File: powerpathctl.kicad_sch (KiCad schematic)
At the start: 10 parts, among them J4 Conn_01x03_Male_BAT_PWR, J5 Conn_01x06_Male, J6 Conn_01x03_Male_BAT_PWR_IN_NU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, J7 Conn_01x06_Male_BAT_data, Q1 SI7149ADP-T1-GE3, U9 LTC4412ES6

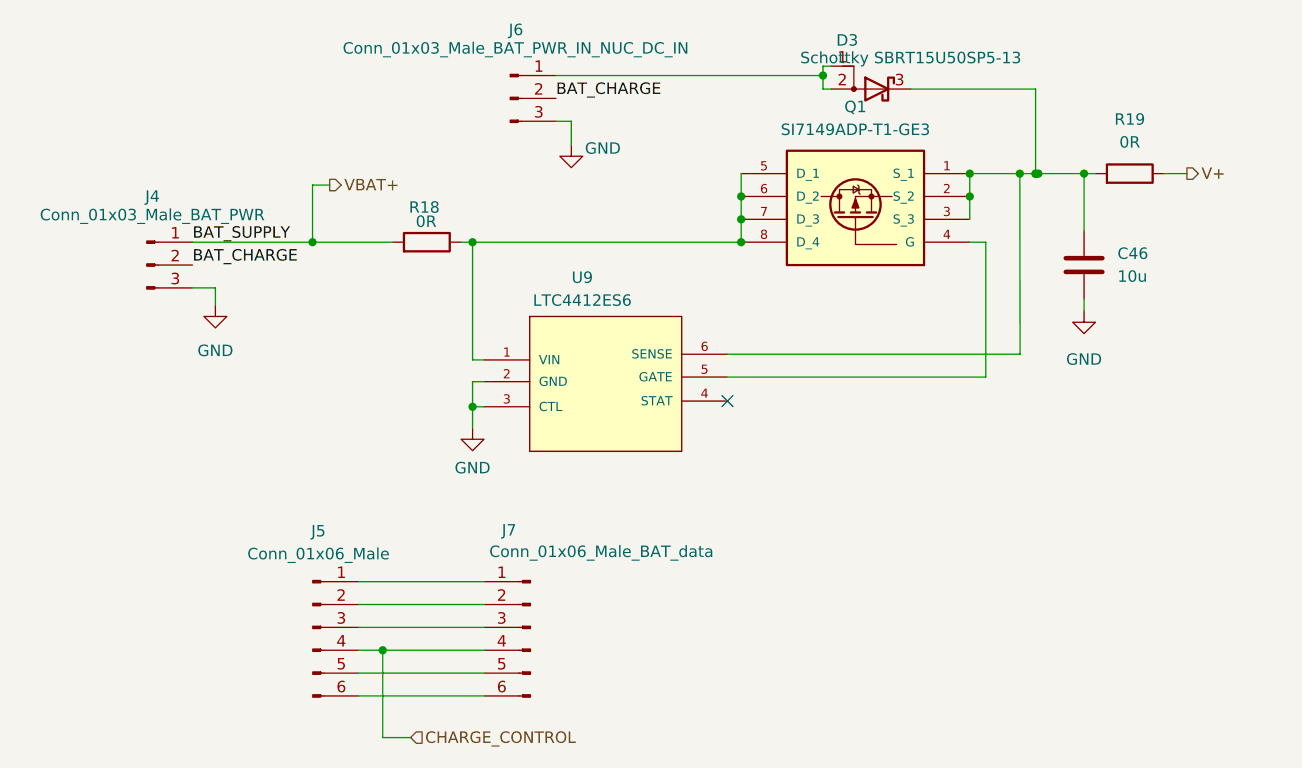
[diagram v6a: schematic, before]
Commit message: replaced main MCU, reannotated
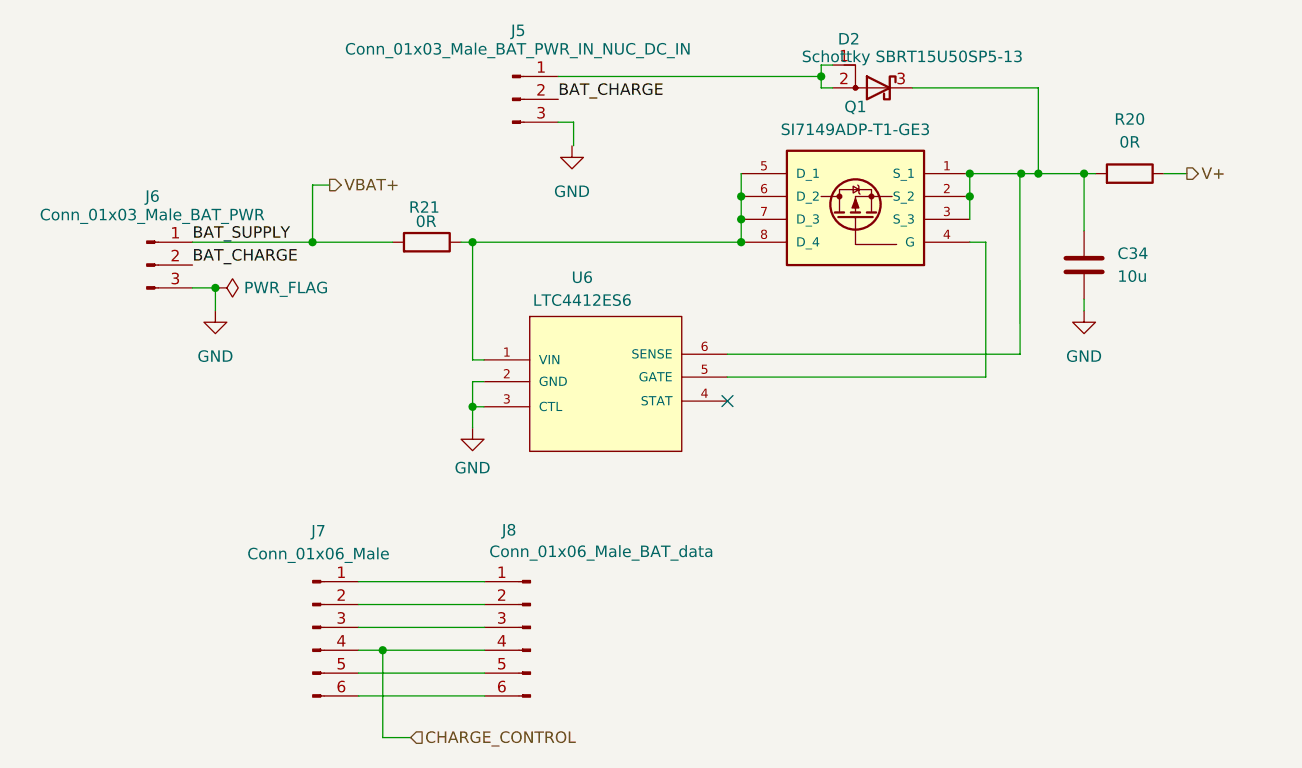
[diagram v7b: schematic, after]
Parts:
- renumbered C46 to C34, D3 to D2, J6 to J5, J4 to J6, J5 to J7, J7 to J8, R19 to R20, R18 to R21, U9 to U6
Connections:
- net GND: no longer J5.3 (Pin_3)
- net at Q1.1 (S_1), Q1.2 (S_2), Q1.3 (S_3)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: no longer C34.1, D2.3 (K), R20.2
- new net: C34.1, D2.3 (K), R20.2

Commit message: resolved all erc errors
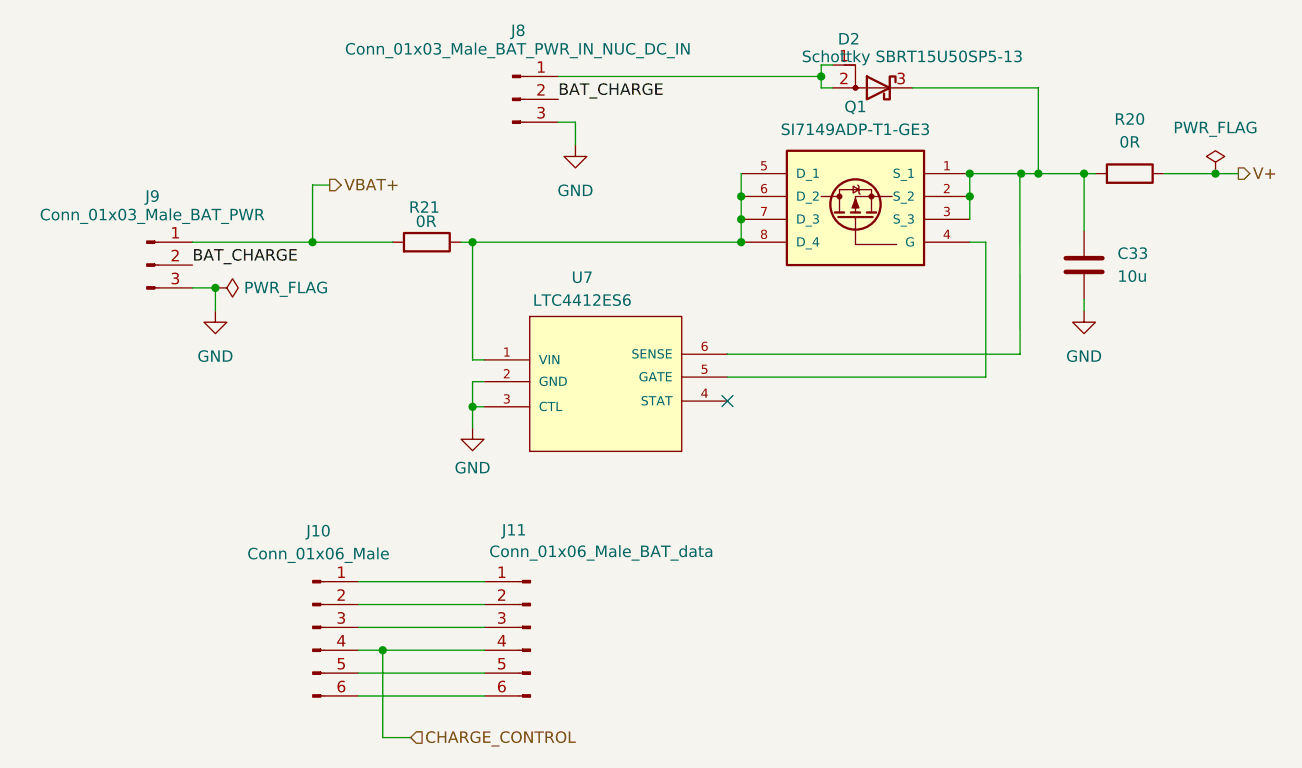
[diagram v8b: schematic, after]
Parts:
- renumbered C34 to C33, J7 to J10, J8 to J11, J5 to J8, J6 to J9, U6 to U7
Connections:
- net GND: now also J8.3 (Pin_3)
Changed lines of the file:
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@@
   (junction (at 176.53 69.85) (diameter 0) (color 0 0 0 0)
   )
+  (junction (at 203.835 67.31) (diameter 0) (color 0 0 0 0)
+  )
   (junction (at 121.285 74.93) (diameter 0) (color 0 0 0 0)
   )
@@
   (junction (at 103.505 74.93) (diameter 0) (color 0 0 0 0)
   )
+  (junction (at 92.71 80.01) (diameter 0) (color 0 0 0 0)
+  )
   (junction (at 182.245 67.31) (diameter 0) (color 0 0 0 0)
   )
   (junction (at 151.13 72.39) (diameter 0) (color 0 0 0 0)
   )
-  (junction (at 92.71 80.01) (diameter 0) (color 0 0 0 0)
-  )
   (no_connect (at 149.606 92.583))
+  (wire (pts (xy 132.715 61.595) (xy 132.715 64.135))
+    (stroke (width 0) (type default) (color 0 0 0 0))
+  )
   (wire (pts (xy 108.6104 117.729) (xy 122.6312 117.729))
     (stroke (width 0) (type default) (color 0 0 0 0))
@@
     (stroke (width 0) (type default) (color 0 0 0 0))
   )
-  (wire (pts (xy 130.81 61.595) (xy 132.5118 61.595))
-    (stroke (width 0) (type default) (color 0 0 0 0))
-  )
   (wire (pts (xy 121.285 90.424) (xy 121.285 93.218))
     (stroke (width 0) (type default) (color 0 0 0 0))
@@
     (stroke (width 0) (type default) (color 0 0 0 0))
   )
-  (wire (pts (xy 132.5118 61.595) (xy 132.5118 64.2112))
-    (stroke (width 0) (type default) (color 0 0 0 0))
-  )
   (wire (pts (xy 121.285 93.218) (xy 122.555 93.218))
     (stroke (width 0) (type default) (color 0 0 0 0))
@@
     (stroke (width 0) (type default) (color 0 0 0 0))
   )
-  (wire (pts (xy 198.12 67.31) (xy 200.66 67.31))
-    (stroke (width 0) (type default) (color 0 0 0 0))
-  )
   (wire (pts (xy 151.13 69.85) (xy 151.13 72.39))
     (stroke (width 0) (type default) (color 0 0 0 0))
@@
     (stroke (width 0) (type default) (color 0 0 0 0))
   )
+  (wire (pts (xy 198.12 67.31) (xy 203.835 67.31))
+    (stroke (width 0) (type default) (color 0 0 0 0))
+  )
   (wire (pts (xy 105.41 68.58) (xy 103.505 68.58))
     (stroke (width 0) (type default) (color 0 0 0 0))
@@
     (stroke (width 0) (type default) (color 0 0 0 0))
   )
+  (wire (pts (xy 203.835 67.31) (xy 206.375 67.31))
+    (stroke (width 0) (type default) (color 0 0 0 0))
+  )
   (wire (pts (xy 108.6104 112.649) (xy 122.6312 112.649))
+    (stroke (width 0) (type default) (color 0 0 0 0))
+  )
+  (wire (pts (xy 130.81 61.595) (xy 132.715 61.595))
     (stroke (width 0) (type default) (color 0 0 0 0))
   )
@@
     (effects (font (size 1.27 1.27)) (justify left bottom))
   )
-  (label "BAT_SUPPLY" (at 90.17 74.93 0)
-    (effects (font (size 1.27 1.27)) (justify left bottom))
-  )
   (hierarchical_label "CHARGE_CONTROL" (shape input) (at 114.4016 129.9718 0)
     (effects (font (size 1.27 1.27)) (justify left))
   )
-  (hierarchical_label "V+" (shape output) (at 200.66 67.31 0)
+  (hierarchical_label "V+" (shape output) (at 206.375 67.31 0)
     (effects (font (size 1.27 1.27)) (justify left))
   )
@@
   (symbol (lib_id "Connector:Conn_01x03_Male") (at 85.09 77.47 0) (unit 1)
     (in_bom yes) (on_board yes)
-    (property "Reference" "J6" (id 0) (at 85.725 69.85 0))
+    (property "Reference" "J9" (id 0) (at 85.725 69.85 0))
     (property "Value" "Conn_01x03_Male_BAT_PWR" (id 1) (at 85.6996 71.9074 0))
     (property "Footprint" "Connector_AMASS:AMASS_MR30PW-M_1x03_P3.50mm_Horizontal" (id 2) (at 85.09 77.47 0)
@@
   (symbol (lib_id "power:GND") (at 92.71 82.55 0) (unit 1)
     (in_bom yes) (on_board yes) (fields_autoplaced)
-    (property "Reference" "#PWR053" (id 0) (at 92.71 88.9 0)
+    (property "Reference" "#PWR049" (id 0) (at 92.71 88.9 0)
       (effects (font (size 1.27 1.27)) hide)
     )
@@
     (pin "2")
   )
-  (symbol (lib_id "power:PWR_FLAG") (at 92.71 80.01 270) (unit 1)
-    (in_bom yes) (on_board yes) (fields_autoplaced)
-    (property "Reference" "#FLG0101" (id 0) (at 94.615 80.01 0)
-      (effects (font (size 1.27 1.27)) hide)
-    )
-    (property "Value" "PWR_FLAG" (id 1) (at 95.885 80.0099 90)
-      (effects (font (size 1.27 1.27)) (justify left))
-    )
-    (property "Footprint" "" (id 2) (at 92.71 80.01 0)
-      (effects (font (size 1.27 1.27)) hide)
-    )
-    (property "Datasheet" "~" (id 3) (at 92.71 80.01 0)
-      (effects (font (size 1.27 1.27)) hide)
-    )
-    (pin "1")
-  )
   (symbol (lib_id "LTC4412ES6:LTC4412ES6") (at 127.635 83.185 0) (unit 1)
     (in_bom yes) (on_board yes)
-    (property "Reference" "U6" (id 0) (at 133.477 78.867 0))
+    (property "Reference" "U7" (id 0) (at 133.477 78.867 0))
     (property "Value" "LTC4412ES6" (id 1) (at 133.477 81.407 0))
     (property "Footprint" "Robotont:TSOT-23_S6" (id 2) (at 120.015 88.011 0)
@@
   (symbol (lib_id "Device:C") (at 189.23 77.47 0) (unit 1)
     (in_bom yes) (on_board yes) (fields_autoplaced)
-    (property "Reference" "C34" (id 0) (at 192.9384 76.1999 0)
+    (property "Reference" "C33" (id 0) (at 192.9384 76.1999 0)
       (effects (font (size 1.27 1.27)) (justify left))
     )
@@
     (pin "2")
   )
-  (symbol (lib_id "power:GND") (at 132.334 64.2366 0) (unit 1)
-    (in_bom yes) (on_board yes) (fields_autoplaced)
-    (property "Reference" "#PWR052" (id 0) (at 132.334 70.5866 0)
-      (effects (font (size 1.27 1.27)) hide)
-    )
-    (property "Value" "GND" (id 1) (at 132.334 69.3166 0))
-    (property "Footprint" "" (id 2) (at 132.334 64.2366 0)
-      (effects (font (size 1.27 1.27)) hide)
-    )
-    (property "Datasheet" "" (id 3) (at 132.334 64.2366 0)
+  (symbol (lib_id "power:GND") (at 132.715 64.135 0) (unit 1)
+    (in_bom yes) (on_board yes) (fields_autoplaced)
+    (property "Reference" "#PWR048" (id 0) (at 132.715 70.485 0)
+      (effects (font (size 1.27 1.27)) hide)
+    )
+    (property "Value" "GND" (id 1) (at 132.715 69.215 0))
+    (property "Footprint" "" (id 2) (at 132.715 64.135 0)
+      (effects (font (size 1.27 1.27)) hide)
+    )
+    (property "Datasheet" "" (id 3) (at 132.715 64.135 0)
       (effects (font (size 1.27 1.27)) hide)
     )
@@
   (symbol (lib_id "Connector:Conn_01x03_Male") (at 125.73 59.055 0) (unit 1)
     (in_bom yes) (on_board yes)
-    (property "Reference" "J5" (id 0) (at 126.365 51.435 0))
+    (property "Reference" "J8" (id 0) (at 126.365 51.435 0))
     (property "Value" "Conn_01x03_Male_BAT_PWR_IN_NUC_DC_IN" (id 1) (at 126.3396 53.4924 0))
     (property "Footprint" "Connector_AMASS:AMASS_MR30PW-M_1x03_P3.50mm_Horizontal" (id 2) (at 125.73 59.055 0)
@@
     (pin "3")
   )
+  (symbol (lib_id "power:PWR_FLAG") (at 203.835 67.31 0) (unit 1)
+    (in_bom yes) (on_board yes) (fields_autoplaced)
+    (property "Reference" "#FLG05" (id 0) (at 203.835 65.405 0)
+      (effects (font (size 1.27 1.27)) hide)
+    )
+    (property "Value" "PWR_FLAG" (id 1) (at 203.835 62.23 0))
+    (property "Footprint" "" (id 2) (at 203.835 67.31 0)
+      (effects (font (size 1.27 1.27)) hide)
+    )
+    (property "Datasheet" "~" (id 3) (at 203.835 67.31 0)
+      (effects (font (size 1.27 1.27)) hide)
+    )
+    (pin "1")
+  )
   (symbol (lib_id "Connector:Conn_01x06_Male") (at 127.7112 117.729 0) (mirror y) (unit 1)
     (in_bom yes) (on_board yes)
-    (property "Reference" "J8" (id 0) (at 124.5362 106.934 0)
+    (property "Reference" "J11" (id 0) (at 124.5362 106.934 0)
       (effects (font (size 1.27 1.27)) (justify right))
     )
@@
   (symbol (lib_id "power:GND") (at 189.23 82.55 0) (unit 1)
     (in_bom yes) (on_board yes) (fields_autoplaced)
-    (property "Reference" "#PWR054" (id 0) (at 189.23 88.9 0)
+    (property "Reference" "#PWR050" (id 0) (at 189.23 88.9 0)
       (effects (font (size 1.27 1.27)) hide)
     )
@@
     (pin "1")
   )
-  (symbol (lib_name "Conn_01x06_Male_1") (lib_id "Connector:Conn_01x06_Male") (at 103.5304 117.729 0) (unit 1)
-    (in_bom yes) (on_board yes) (fields_autoplaced)
-    (property "Reference" "J7" (id 0) (at 104.1654 107.0356 0))
+  (symbol (lib_id "Connector:Conn_01x06_Male") (at 103.5304 117.729 0) (unit 1)
+    (in_bom yes) (on_board yes) (fields_autoplaced)
+    (property "Reference" "J10" (id 0) (at 104.1654 107.0356 0))
     (property "Value" "Conn_01x06_Male " (id 1) (at 104.1654 109.5756 0))
     (property "Footprint" "Connector_JST:JST_PH_S6B-PH-K_1x06_P2.00mm_Horizontal" (id 2) (at 103.5304 117.729 0)
       (effects (font (size 1.27 1.27)) hide)
     )
-    (property "Datasheet" "" (id 3) (at 104.4448 118.6942 0)
+    (property "Datasheet" "~" (id 3) (at 104.4448 118.6942 0)
       (effects (font (size 1.27 1.27)) hide)
     )
@@
   (symbol (lib_id "power:GND") (at 121.285 95.5548 0) (unit 1)
     (in_bom yes) (on_board yes) (fields_autoplaced)
-    (property "Reference" "#PWR055" (id 0) (at 121.285 101.9048 0)
+    (property "Reference" "#PWR051" (id 0) (at 121.285 101.9048 0)
       (effects (font (size 1.27 1.27)) hide)
     )
@@
       (effects (font (size 1.27 1.27)) hide)
     )
+    (pin "1")
+  )
+  (symbol (lib_id "power:PWR_FLAG") (at 92.71 80.01 270) (unit 1)
+    (in_bom yes) (on_board yes) (fields_autoplaced)
+    (property "Reference" "#FLG06" (id 0) (at 94.615 80.01 0)
+      (effects (font (size 1.27 1.27)) hide)
+    )
+    (property "Value" "PWR_FLAG" (id 1) (at 95.885 80.0099 90)
+      (effects (font (size 1.27 1.27)) (justify left))
+    )
+    (property "Footprint" "" (id 2) (at 92.71 80.01 0)
+      (effects (font (size 1.27 1.27)) hide)
+    )
+    (property "Datasheet" "~" (id 3) (at 92.71 80.01 0)
+      (effects (font (size 1.27 1.27)) hide)
+    )
